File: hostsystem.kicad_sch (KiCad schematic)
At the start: 78 parts, among them J1001 TC2050, J1002 Conn_01x03_Pin, U1001 AM6231ASGGGAALW, U1002 SN74LVC2G241DCUR, U1003 AT24C32D-STUM-T, X1001 32.768kHz, X1002 25MHz

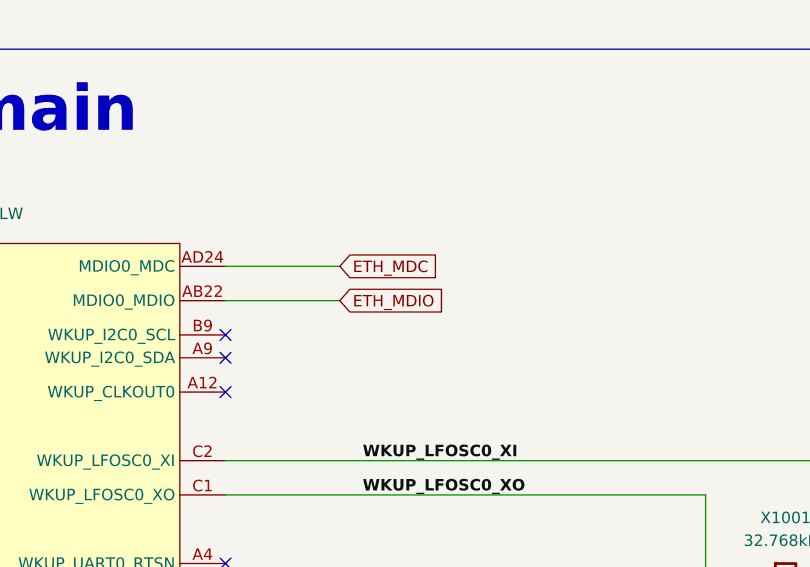
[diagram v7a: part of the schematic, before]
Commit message: More SoC decaps
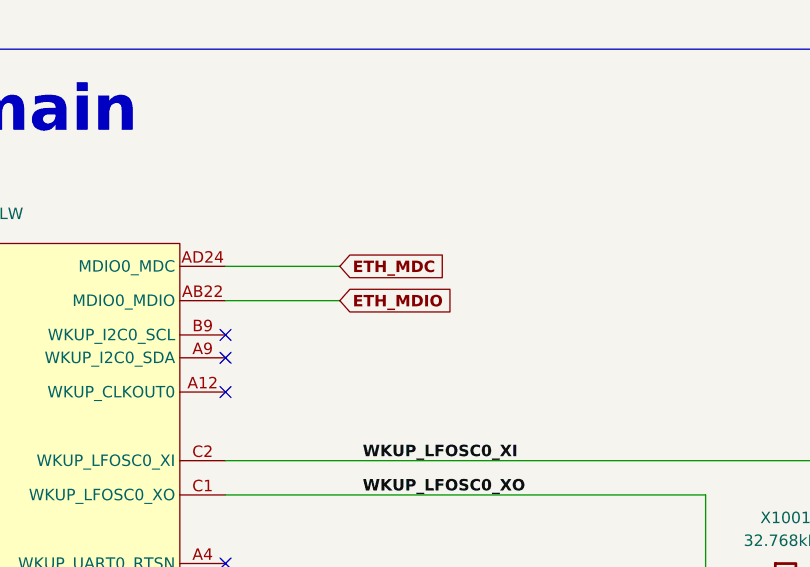
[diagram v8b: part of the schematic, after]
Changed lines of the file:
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@@
 			(font
 				(size 1.27 1.27)
+				(thickness 0.254)
+				(bold yes)
 			)
 			(justify left)
 		)
 		(property "Intersheetrefs" "${INTERSHEET_REFS}"
-			(at 146.6766 311.15 0)
+			(at 147.1526 311.15 0)
 			(effects
 				(font
@@
 			(font
 				(size 1.27 1.27)
+				(thickness 0.254)
+				(bold yes)
 			)
 			(justify left)
 		)
 		(property "Intersheetrefs" "${INTERSHEET_REFS}"
-			(at 146.0113 307.34 0)
-			(effects
-				(font
+			(at 146.4873 307.34 0)
+			(effects
+				(font
